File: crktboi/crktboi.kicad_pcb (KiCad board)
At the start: 2 copper layers, 50 x 50 mm, 10 parts, among them Q1 BC847, Q2 BC847, Q3 2N7002, U1 GSC1102YB-3V4000

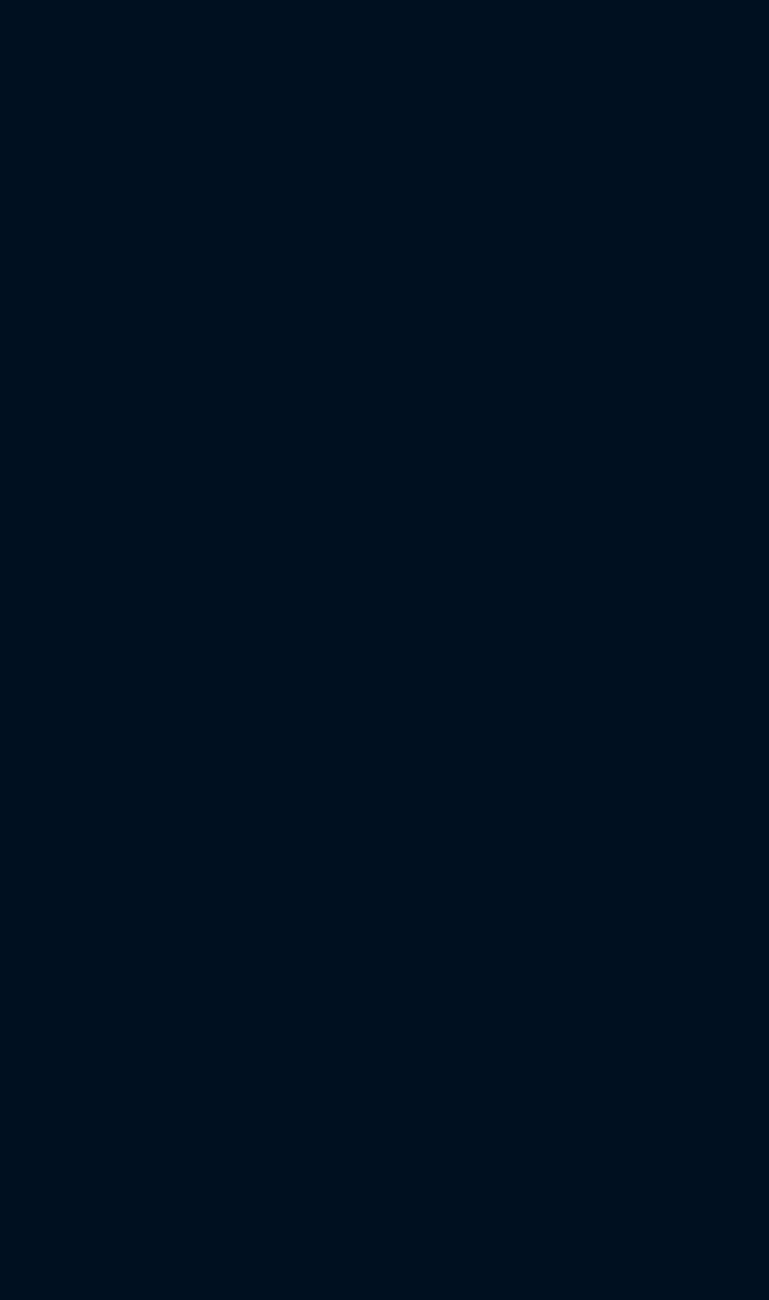
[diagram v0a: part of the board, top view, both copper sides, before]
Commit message: Added a plan document & updated  design with tweaks for 3S3P photodiodes
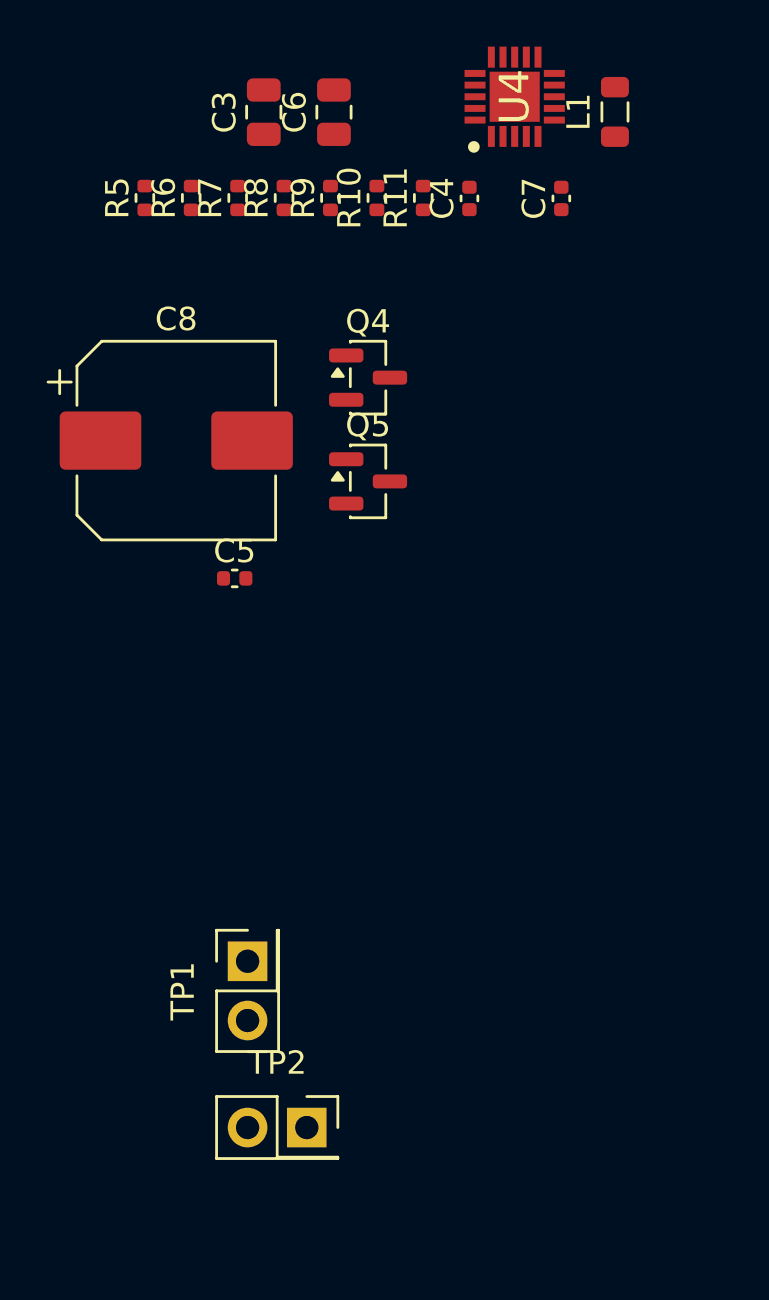
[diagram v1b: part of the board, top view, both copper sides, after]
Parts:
- added C3: 10uF, Capacitor_SMD:C_0805_2012Metric, F.Cu at (84.6, 67.1)
- added C4: 10nF, Capacitor_SMD:C_0402_1005Metric, F.Cu at (93.4, 70.8)
- added C5: 10nF, Capacitor_SMD:C_0402_1005Metric, F.Cu at (83.3, 87.1)
- added C6: 10uF, Capacitor_SMD:C_0805_2012Metric, F.Cu at (87.6, 67.1)
- added C7: 10nF, Capacitor_SMD:C_0402_1005Metric, F.Cu at (97.4, 70.8)
- added C8: 1000uF, 6.3V, Capacitor_SMD:CP_Elec_8x10, F.Cu at (80.8, 81.2)
- added L1: 22uH, Inductor_SMD:L_0805_2012Metric, F.Cu at (99.7, 67.1)
- added Q4: 2N7002, Package_TO_SOT_SMD:SOT-23, F.Cu at (89.1, 78.5)
- added Q5: AO3401A, Package_TO_SOT_SMD:SOT-23, F.Cu at (89.1, 83.0)
- added R10: 6.8 MR, Resistor_SMD:R_0402_1005Metric, F.Cu at (89.4, 70.8)
- added R11: 5.1 MR, Resistor_SMD:R_0402_1005Metric, F.Cu at (91.4, 70.8)
- added R5: 5.11 MR, Resistor_SMD:R_0402_1005Metric, F.Cu at (79.5, 70.8)
- added R6: 5.11 MR, Resistor_SMD:R_0402_1005Metric, F.Cu at (81.5, 70.8)
- added R7: 6.2 MR, Resistor_SMD:R_0402_1005Metric, F.Cu at (83.5, 70.8)
- added R8: 7.5 MR, Resistor_SMD:R_0402_1005Metric, F.Cu at (85.5, 70.8)
- added R9: 1.5 MR, Resistor_SMD:R_0402_1005Metric, F.Cu at (87.5, 70.8)
- added TP1: TestPoint_2Pole, Connector_PinSocket_2.54mm:PinSocket_2x01_P2.54mm_Vertical, F.Cu at (83.9, 103.5)
- added TP2: TestPoint_2Pole, Connector_PinSocket_2.54mm:PinSocket_2x01_P2.54mm_Vertical, F.Cu at (86.4, 110.7)
- added U4: BQ25505RGRT, BQ25505RGRR:QFN50P350X350X100-21N-D, F.Cu at (95.4, 66.5)

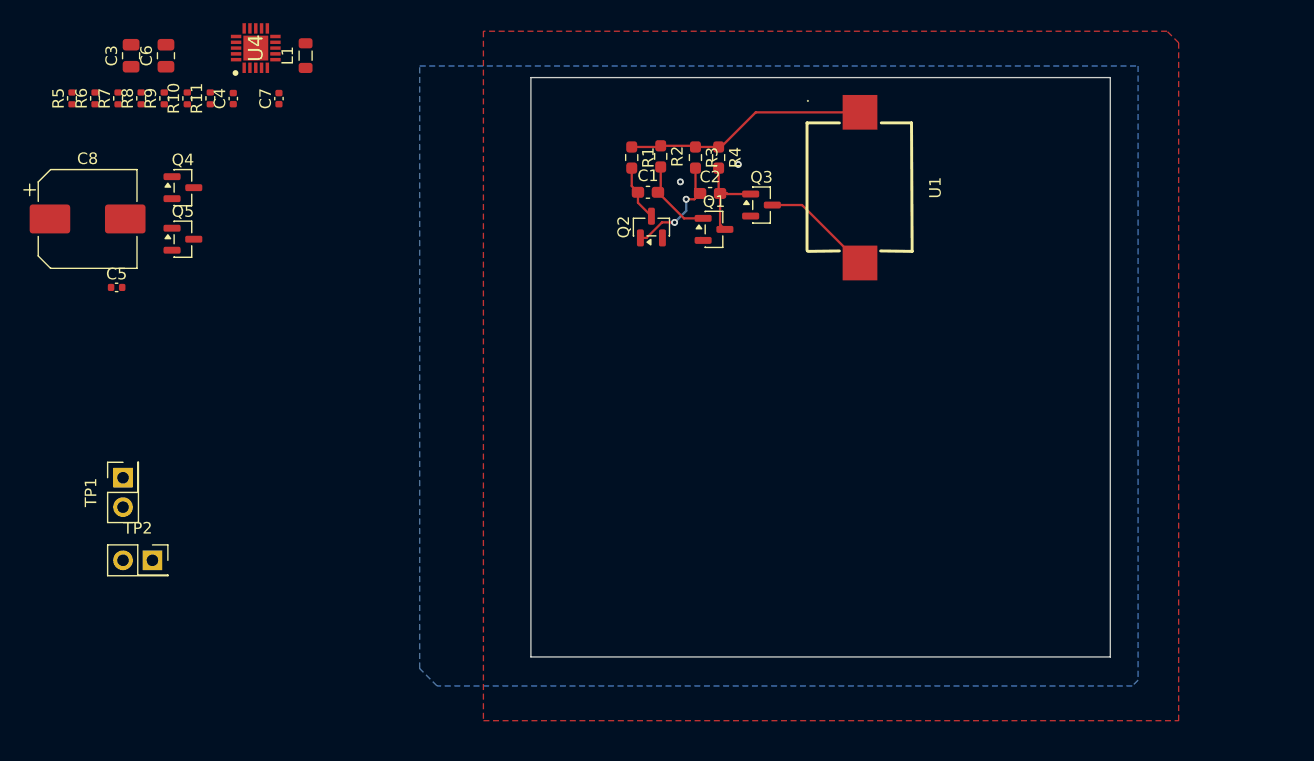
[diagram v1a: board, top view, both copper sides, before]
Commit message: Updated PCB layout with all parts I think we need for power.
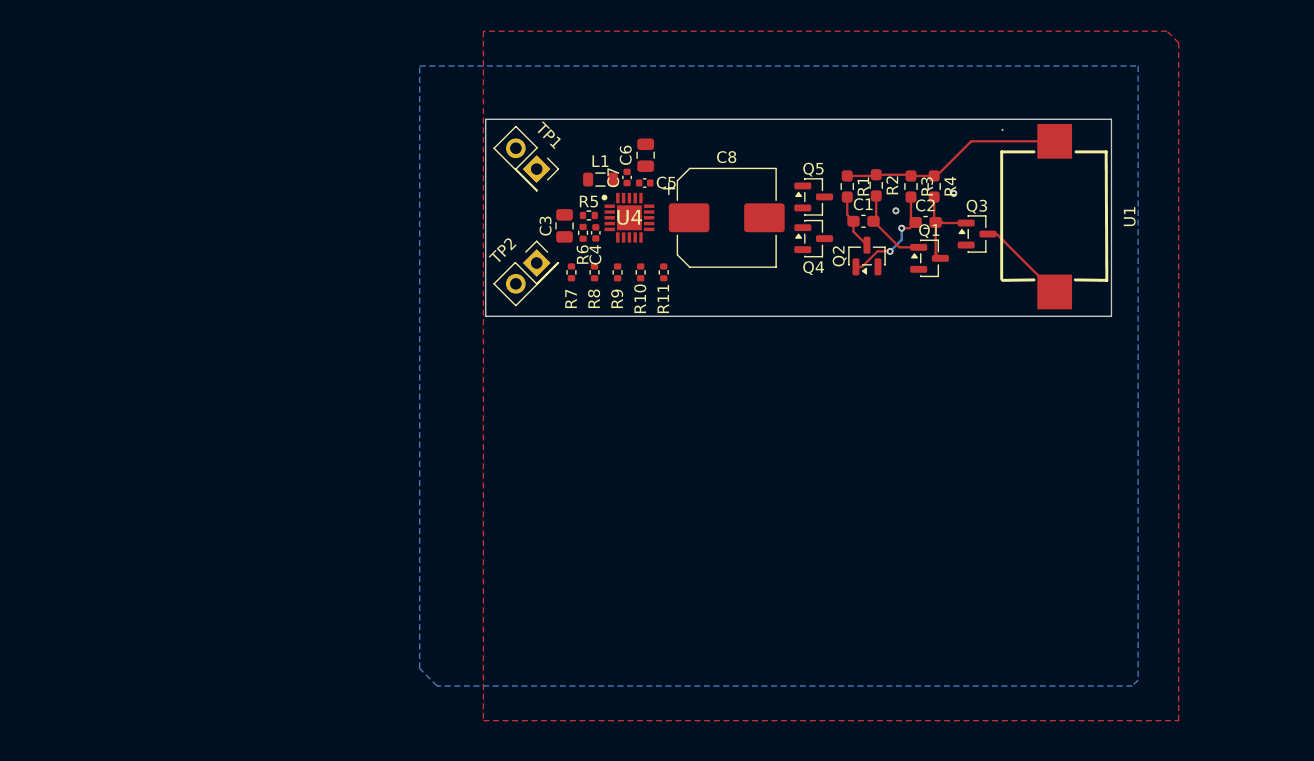
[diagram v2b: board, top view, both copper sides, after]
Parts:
- moved C8 55.2 mm to (136.0, 81.1)
- moved Q4 54.6 mm to (143.5, 82.9)
- moved Q5 54.6 mm to (143.5, 79.3)
- moved C5 46.5 mm to (128.9, 78.1)
- moved R5 45.7 mm to (124.1, 80.9), turned to 0 degrees
- moved TP1 44.5 mm to (119.6, 76.9), turned to -45 degrees
- moved R6 43.7 mm to (123.6, 82.4), turned to -90 degrees
- moved C6 42.3 mm to (129.0, 75.7)
- moved TP2 41.9 mm to (119.6, 85.0), turned to 45 degrees
- moved R10 41.9 mm to (128.6, 85.8), turned to -90 degrees
- moved R11 41.9 mm to (130.6, 85.8), turned to -90 degrees
- moved R7 41.9 mm to (122.6, 85.8), turned to -90 degrees
- moved R8 41.9 mm to (124.6, 85.8), turned to -90 degrees
- moved R9 41.9 mm to (126.6, 85.8), turned to -90 degrees
- moved C3 40.2 mm to (122.0, 81.8), turned to -90 degrees
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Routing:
- net Net-(Q3-D): track 9.63 -> 7.07 mm
- net +3V0: track 21.0 -> 19.2 mm
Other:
- board size 50 x 50 mm -> 54 x 17 mm

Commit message: Changed the shape to be a bit more like a cicada. Added 3D models to parts missing their assignment
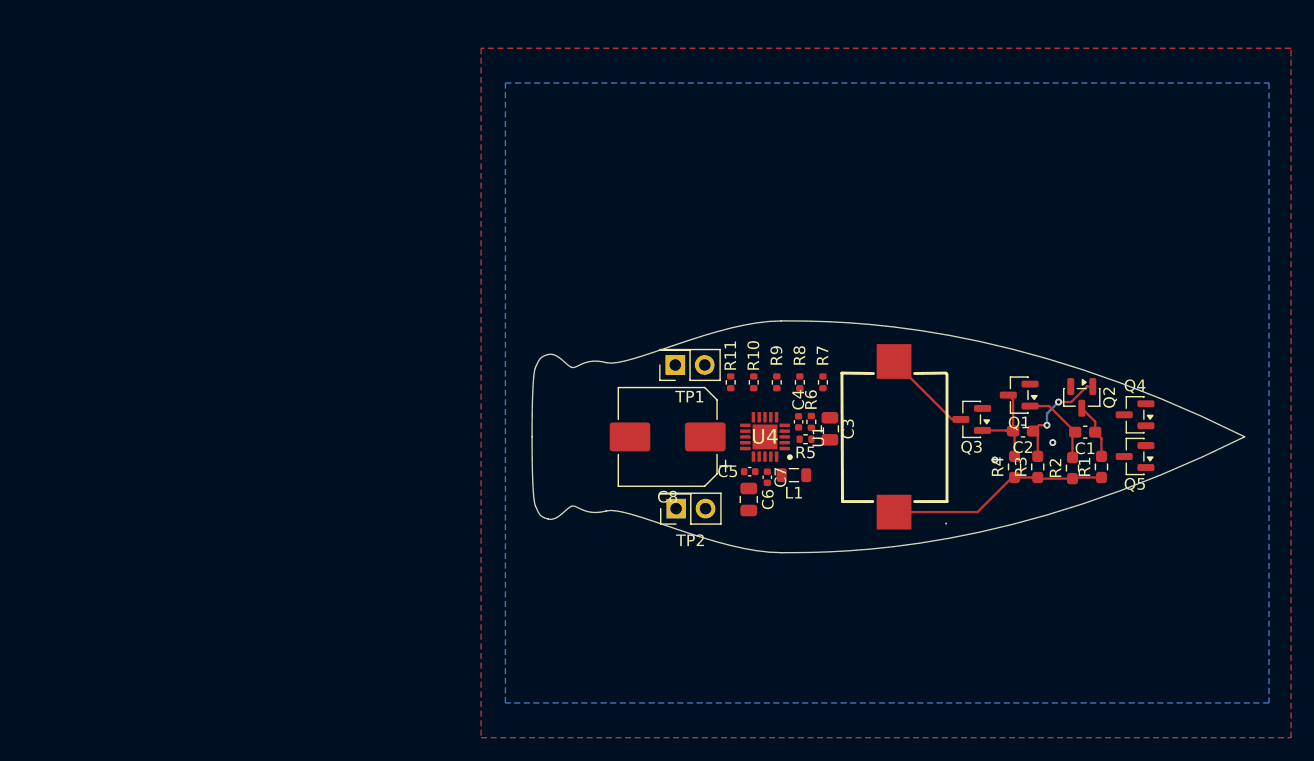
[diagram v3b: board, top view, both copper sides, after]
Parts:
- moved Q5 35.7 mm to (171.2, 101.7), turned to 180 degrees
- moved R1 32.7 mm to (168.3, 102.6), turned to 90 degrees
- moved Q4 31.6 mm to (171.2, 98.1), turned to 180 degrees
- moved C6 31.0 mm to (137.9, 105.4), turned to -90 degrees
- moved L1 30.5 mm to (141.8, 103.3), turned to 180 degrees
- moved R2 29.7 mm to (165.8, 102.7), turned to 90 degrees
- moved C3 28.8 mm to (144.9, 99.3), turned to 90 degrees
- moved C7 28.6 mm to (139.5, 103.5), turned to -90 degrees
- moved R5 26.9 mm to (142.8, 100.2), turned to 180 degrees
- moved R3 26.6 mm to (162.8, 102.6), turned to 90 degrees
- moved C5 26.5 mm to (138.0, 103.0), turned to 180 degrees
- moved C1 26.4 mm to (166.9, 99.6), turned to 180 degrees
- moved R6 25.6 mm to (143.3, 98.7), turned to 90 degrees
- moved R4 25.2 mm to (160.8, 102.6), turned to 90 degrees
- moved TP2 24.4 mm to (131.6, 106.2), turned to 180 degrees
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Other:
- board size 54 x 17 mm -> 61.5 x 20 mm

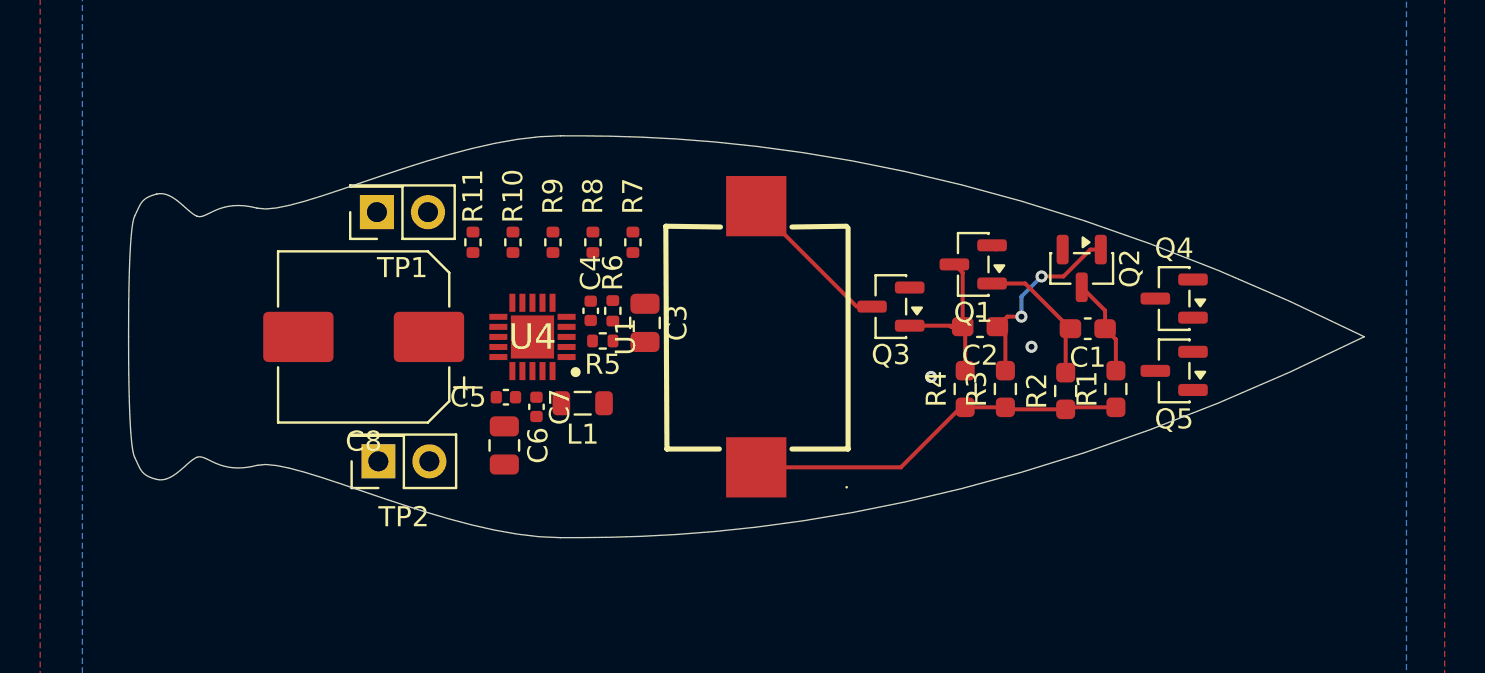
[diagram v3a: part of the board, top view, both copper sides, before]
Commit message: Added photodiodes to the base design for eyes on the cicada.
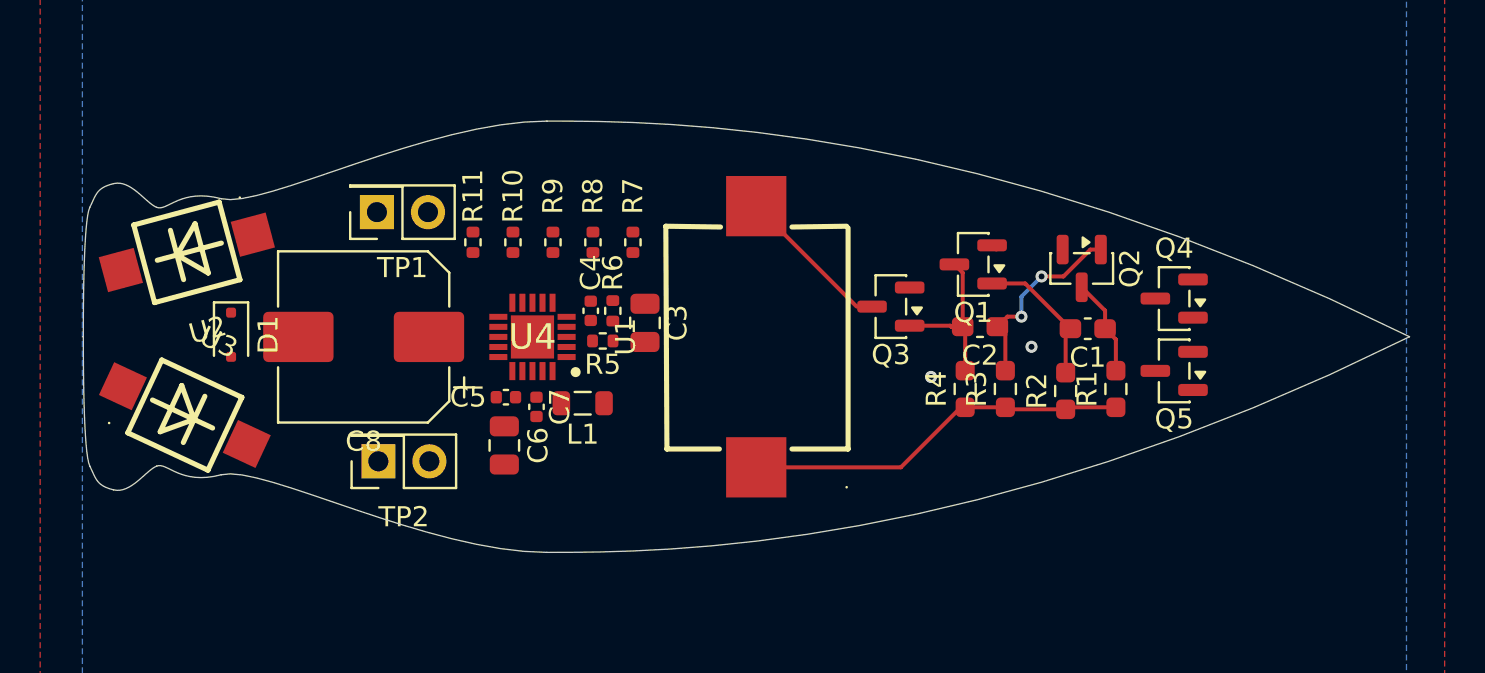
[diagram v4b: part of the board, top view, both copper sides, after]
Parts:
- added D1: BAT54J, Diode_SMD:D_SOD-323F, F.Cu at (124.3, 99.9)
- added U2: VBPW34S, VBPW34S:SENSOR-SMD_L4.4-W3.9, F.Cu at (122.1, 95.8)
- added U3: VBPW34S, VBPW34S:SENSOR-SMD_L4.4-W3.9, F.Cu at (122.0, 103.9)
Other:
- board size 61.5 x 20 mm -> 66 x 21.5 mm
